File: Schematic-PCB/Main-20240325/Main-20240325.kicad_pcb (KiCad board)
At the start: 4 copper layers, 112 x 112 mm, 102 parts, among them J1 Conn_PWR, J2 CamS3-4, J3 CamS3-6, J4 Pixy 2.1, J5 Conn_MD, J6 Conn_Dribbler, J7 Conn_UI, J8 Conn_NeoPixel, SW1 Cam_RST, SW2 Main_RST, SW3 Sub_RST, SW4 SW_DPDT_x2, U1 DEV-16771, U10 TSSP4038, U11 TSSP4038, U12 TSSP4038, U13 TSSP4038, U14 TSSP4038, U15 TSSP4038, U16 TSSP4038, U17 TSSP4038, U19 ESP32-DEVKITC, U2 TSSP4038, U20 TSSP4038, U21 TSSP4038, U22 TSSP4038, U23 TSSP4038, U3 TSSP4038, U4 TSSP4038, U5 TSSP4038, U6 TSSP4038, U7 TSSP4038, U8 TSSP4038, U9 TSSP4038

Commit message: update: メイン基板を更新した
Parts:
- removed R28: 10, Resistor_SMD:R_0603_1608Metric
- removed R29: 510, Resistor_SMD:R_0603_1608Metric
- RV1: value 1K -> 10K
- moved U1 1.09 mm to (0.00, -1.09)
- moved U19 1.09 mm to (0.00, -1.09)
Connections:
- net Volume renamed Net-(R30-Pad1)
- J3 pad 1: Cam-EN -> unconnected-(J3-Pin_1-Pad1)
- J3 pad 2: unconnected-(J3-Pin_2-Pad2) -> Cam-EN
- RV1 pad 1: Net-(R28-Pad2) -> +3.3V
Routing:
- net +3.3V: track 59.0 -> 85.2 mm
- net Net-(R28-Pad2): track 3.00 -> 0.00 mm
- net Net-(R28-Pad1): track 2.00 -> 0.00 mm
- net SDA: track 19.9 -> 21.0 mm
- net SCL: track 25.3 -> 26.4 mm

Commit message: clean: コンフリクトを修正
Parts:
- removed J8: Conn_NeoPixel, @2024TOINIOT2-Main:Connector
- added REF**: MountingHole_3.2mm_M3, MountingHole:MountingHole_3.2mm_M3, F.Cu at (23.6, -35.3)
- added REF**: MountingHole_3.2mm_M3, MountingHole:MountingHole_3.2mm_M3, F.Cu at (23.6, 35.3)
- added REF**: MountingHole_3.2mm_M3, MountingHole:MountingHole_3.2mm_M3, F.Cu at (-23.7, -35.5)
- moved J6 3.40 mm to (22.6, -19.7)
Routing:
- net +5V: track 49.9 -> 46.3 mm
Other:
- board text removed: "A0"
- board text removed: "A1"
- board text removed: "A12"
- board text removed: "A13"
- board text removed: "A14"
- board text removed: "A15"
- board text removed: "A16"
- board text removed: "A17"
- board text removed: "A2"
- board text removed: "A3"
- board text removed: "A4"
- board text removed: "A5"
- board text removed: "A6"
- board text removed: "A7"
- board text removed: "A8"
- board text removed: "A9"

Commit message: update: メイン基板のPCBで部品配置を進めた
ESP32C3にしたら結構配置がいい感じに決まった...のか？
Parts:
- removed R26, R27: 330, Resistor_SMD:R_0603_1608Metric
- removed the REF** at (30.1, -30.1)
- removed the REF** at (30.1, 30.1)
- removed the REF** at (23.6, -35.3)
- removed the REF** at (23.6, 35.3)
- removed the REF** at (-23.7, -35.5)
- removed the REF** at (-30.1, 30.1)
- removed the REF** at (-30.1, -30.1)
- removed SW3: Sub_RST, @2024TOINIOT2-Line:Tactile1
- removed U20, U21, U22, U23: TSSP4038, OptoDevice:Vishay_MINICAST-3Pin
- added J8: Conn_NeoPixel, @2024TOINIOT2-Main:Connector, F.Cu at (0.00, -46.0)
- added REF**: MountingHole_3.2mm_M3, MountingHole:MountingHole_3.2mm_M3, F.Cu at (30.1, 30.1)
- added REF**: MountingHole_3.2mm_M3, MountingHole:MountingHole_3.2mm_M3, F.Cu at (-30.1, 30.1)
- added REF**: MountingHole_3.2mm_M3, MountingHole:MountingHole_3.2mm_M3, F.Cu at (-23.6, -35.3)
- added REF**: MountingHole_3.2mm_M3, MountingHole:MountingHole_3.2mm_M3, F.Cu at (23.6, -35.3)
- added REF**: MountingHole_3.2mm_M3, MountingHole:MountingHole_3.2mm_M3, F.Cu at (23.6, 35.3)
- added REF**: MountingHole_3.2mm_M3, MountingHole:MountingHole_3.2mm_M3, F.Cu at (-23.6, 35.3)
- added REF**: MountingHole_3.2mm_M3, MountingHole:MountingHole_3.2mm_M3, F.Cu at (30.1, -30.1)
- added REF**: MountingHole_3.2mm_M3, MountingHole:MountingHole_3.2mm_M3, F.Cu at (-30.1, -30.1)
- added SW5: Cam_RST, @2024TOINIOT2-Line:Tactile1, F.Cu at (186.5, 120.0)
- C1, C2: moved to F.Cu
- C10, C11, C12, C9: value 0.33uF -> 0.1uF
- D1: value PWR-5 -> BLTIN; footprint LED_SMD:LED_0805_2012Metric -> LED_SMD:LED_0603_1608Metric
- D2: value PWR-3.3 -> BLTIN; footprint LED_SMD:LED_0805_2012Metric -> LED_SMD:LED_0603_1608Metric
- D3: value D_Small -> PWR-5; footprint Diode_THT:D_A-405_P7.62mm_Horizontal -> LED_SMD:LED_0603_1608Metric
- D4: value BLTIN -> PWR-3.3
- D5: value BLTIN -> D_Small; footprint LED_SMD:LED_0603_1608Metric -> Diode_THT:D_A-405_P7.62mm_Horizontal
- J3: footprint Connector_PinSocket_2.54mm:PinSocket_2x03_P2.54mm_Vertical -> Connector_PinHeader_2.54mm:PinHeader_2x03_P2.54mm_Vertical
- R1: value 10K -> 330
- R16, R17, R6: value 39K -> 10K
- R20, R21: value 1K -> 39K
- R3: value 330 -> 1K
- R4: value 39K -> 1K
- R5, R7: value 39K -> 330
- RV1: footprint @2024-Main:3362P -> @2024TOINIOT2-Main:3362P
- SW1: value Cam_RST -> SW_DPDT_x2; footprint @2024TOINIOT2-Line:Tactile1 -> @2024TOINIOT2-Main:2MD1-T2-B4-M2-Q-N; moved to B.Cu
- SW4: value SW_DPDT_x2 -> Cam_RST; footprint @2024-Main:2MD1T2B4M2QN -> @2024TOINIOT2-Line:Tactile1; moved to F.Cu
- U10, U11, U12, U13, U14, U15, U16, U17, U3, U4, U5, U6, U7, U8, U9: footprint @2024TOINIOT2-Main:Vishay_MINICAST-3Pin -> @2024TOINIOT2-Main:TSSP4038
- U18: value ~ -> TSSP4038; footprint @2024TOINIOT2-Main:BNO055 -> @2024TOINIOT2-Main:TSSP4038
- U19: value ESP32-DEVKITC -> ~; footprint @2024TOINIOT2-Main:ESP32-DEVKITC -> @2024TOINIOT2-Main:XIAO ESP32C3
- U2: value TSSP4038 -> ~; footprint @2024TOINIOT2-Main:Vishay_MINICAST-3Pin -> @2024TOINIOT2-Main:BNO055; moved to F.Cu
- moved SW4 237.2 mm to (186.5, 114.5), turned to 0 degrees
- moved C2 225.5 mm to (161.8, 123.7)
- moved C1 213.3 mm to (161.8, 112.1)
- moved SW2 188.0 mm to (186.5, 109.0), turned to 0 degrees
- moved RV1 173.0 mm to (162.4, 133.7), turned to 0 degrees
- moved D3 165.7 mm to (134.0, 131.8), turned to 0 degrees
- moved SW1 72.0 mm to (-33.3, 22.2), turned to 123.75 degrees
- moved D1 49.7 mm to (134.0, 126.6)
- moved U18 49.5 mm to (18.9, -45.7), turned to -22.5 degrees
- moved D2 49.3 mm to (134.0, 129.2)
- moved D5 46.1 mm to (181.3, 90.5)
- moved J4 41.1 mm to (-16.3, -5.08), turned to 0 degrees
- moved J2 38.9 mm to (-12.0, 21.0)
- moved J3 38.0 mm to (-17.5, 15.3)
- moved U2 33.8 mm to (17.0, -20.3)
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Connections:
- C10 pad 1: ball02 -> +3.3V
- C11 pad 1: ball03 -> +5V
- C12 pad 1: ball04 -> +5V
- C13 pad 1: ball05 -> ball01
- C14 pad 1: ball06 -> ball02
- C15 pad 1: ball07 -> ball03
- C16 pad 1: ball08 -> ball04
- C17 pad 1: ball09 -> ball05
- C18 pad 1: ball10 -> ball06
- C19 pad 1: ball11 -> ball07
- C20 pad 1: ball12 -> ball08
- C21 pad 1: ball13 -> ball09
- C22 pad 1: ball14 -> ball10
- C23 pad 1: ball15 -> ball11
- C24 pad 1: ball16 -> ball12
- C25 pad 1: ball-a-01 -> ball13
- C26 pad 1: ball-a-02 -> ball14
- C27 pad 1: ball-a-03 -> ball15
- C28 pad 1: ball-a-04 -> ball16
- C9 pad 1: ball01 -> +5V
- D3 pad 1: Net-(D3-K) -> GND
- D3 pad 2: +5V -> Net-(D3-A)
- D5 pad 1: GND -> Net-(D5-K)
- D5 pad 2: Net-(D5-A) -> +5V
- J3 pad 1: unconnected-(J3-Pin_1-Pad1) -> Cam_EN
- J3 pad 2: Cam-EN -> Cam_G0
- J3 pad 4: +5V -> Cam-RX
- J3 pad 6: Cam-RX -> +5V
- R1 pad 1: +5V -> SCK
- R1 pad 2: Cam-EN -> Net-(D1-A)
- R10 pad 1: Net-(U8-OUT) -> Net-(U5-OUT)
- R10 pad 2: ball07 -> ball03
- R11 pad 1: Net-(U9-OUT) -> Net-(U6-OUT)
- R11 pad 2: ball08 -> ball04
- R12 pad 1: Net-(U10-OUT) -> Net-(U7-OUT)
- R12 pad 2: ball09 -> ball05
- R13 pad 1: Net-(U11-OUT) -> Net-(U8-OUT)
- R13 pad 2: ball10 -> ball06
- R14 pad 1: Net-(U12-OUT) -> Net-(U9-OUT)
- R14 pad 2: ball11 -> ball07
- R15 pad 1: Net-(U13-OUT) -> Net-(U10-OUT)
- R15 pad 2: ball12 -> ball08
- R16 pad 1: Net-(U14-OUT) -> +3.3V
- R16 pad 2: ball13 -> Cam_EN
- R17 pad 1: Net-(U15-OUT) -> +3.3V
- R17 pad 2: ball14 -> Cam_G0
- R18 pad 1: Net-(U16-OUT) -> Net-(U11-OUT)
- R18 pad 2: ball15 -> ball09
- R19 pad 1: Net-(U17-OUT) -> Net-(U12-OUT)
- R19 pad 2: ball16 -> ball10
- R2 pad 1: +5V -> Sub_BLTIN
- R2 pad 2: Net-(D1-A) -> Net-(D2-A)
- R20 pad 1: +3.3V -> Net-(U13-OUT)
- R20 pad 2: SDA -> ball11
- R21 pad 1: +3.3V -> Net-(U14-OUT)
- R21 pad 2: SCL -> ball12
- R22 pad 1: Net-(U20-OUT) -> Net-(U15-OUT)
- R22 pad 2: ball-a-01 -> ball13
- R23 pad 1: Net-(U21-OUT) -> Net-(U16-OUT)
- R23 pad 2: ball-a-02 -> ball14
- R24 pad 1: Net-(U22-OUT) -> Net-(U17-OUT)
- R24 pad 2: ball-a-03 -> ball15
- R25 pad 1: Net-(U23-OUT) -> Net-(U18-OUT)
- R25 pad 2: ball-a-04 -> ball16
- R3 pad 2: Net-(D2-A) -> SDA
- R4 pad 1: Net-(U2-OUT) -> +3.3V
- R4 pad 2: ball01 -> SCL
- R5 pad 1: Net-(U3-OUT) -> +5V
- R5 pad 2: ball02 -> Net-(D3-A)
- R6 pad 1: Net-(U4-OUT) -> Net-(R6-Pad1)
- R6 pad 2: ball03 -> Volume
- R7 pad 1: Net-(U5-OUT) -> +3.3V
- R7 pad 2: ball04 -> Net-(D4-A)
- R8 pad 1: Net-(U6-OUT) -> Net-(U3-OUT)
- R8 pad 2: ball05 -> ball01
- R9 pad 1: Net-(U7-OUT) -> Net-(U4-OUT)
- R9 pad 2: ball06 -> ball02
- RV1 pad 2: Net-(R30-Pad1) -> Net-(R6-Pad1)
- SW1 pad 1: GND -> +5V
- SW1 pad 2: Cam-EN -> 5.0V
- SW4 pad 1: +5V -> GND
- SW4 pad 2: 5.0V -> Cam_EN
- U1 pad 3.3V: +3.3V -> unconnected-(U1-Pad3.3V)
- U18 pad 1: +3.3V -> Net-(U18-OUT)
- U18 pad 3: SDA -> +3.3V
- U19 pad 1: unconnected-(U19-3V3-Pad1) -> ball01k
- U19 pad 10: KickerSignal -> unconnected-(U19-MISO_D9-Pad10)
- U19 pad 11: PH-D -> NeoPixel_PWM
- U19 pad 12: EN-D -> unconnected-(U19-3V3-Pad12)
- U19 pad 13: unconnected-(U19-12_A15-Pad13) -> GND
- U19 pad 14: GND -> Net-(D5-K)
- U19 pad 2: Sub_RST -> ball02k
- U19 pad 3: ball01k -> KickerSignal
- U19 pad 4: ball02k -> Volume
- U19 pad 5: ball-a-01 -> PH-D
- U19 pad 6: ball-a-02 -> EN-D
- U19 pad 7: ball-a-03 -> Main-RX7
- U19 pad 8: ball-a-04 -> Main-TX7
- U19 pad 9: NeoPixel_PWM -> Sub_BLTIN
- U2 pad 1: Net-(U2-OUT) -> +3.3V
- U2 pad 3: +3.3V -> SDA
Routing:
- net +3.3V: track 85.2 -> 0.00 mm
- net +5V: track 46.3 -> 0.00 mm
- net 3.3V: track 22.6 -> 0.00 mm
- net SCL: track 26.4 -> 9.93 mm
- net SDA: track 21.0 -> 9.93 mm
- net 5.0V: track 9.33 -> 0.00 mm
- removed copper zone on B.Cu, net GND
- removed copper zone on F.Cu, net GND
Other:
- outline, holes or cut-outs redrawn

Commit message: update: メイン基板の回路図/PCBを更新
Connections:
- U19 pad 3: KickerSignal -> Volume
- U19 pad 4: Volume -> KickerSignal

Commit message: update: 部品配置を進めた
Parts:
- C1, C2: moved to B.Cu
- moved C2 232.0 mm to (-29.9, -7.05)
- moved C1 219.8 mm to (-29.9, 4.50)
- moved SW5 186.3 mm to (37.5, 8.20), turned to 180 degrees
- moved SW4 180.0 mm to (37.5, 13.7), turned to 180 degrees
- moved RV1 179.9 mm to (42.0, 0.00), turned to 90 degrees
- moved SW2 174.1 mm to (37.5, 19.1), turned to 180 degrees

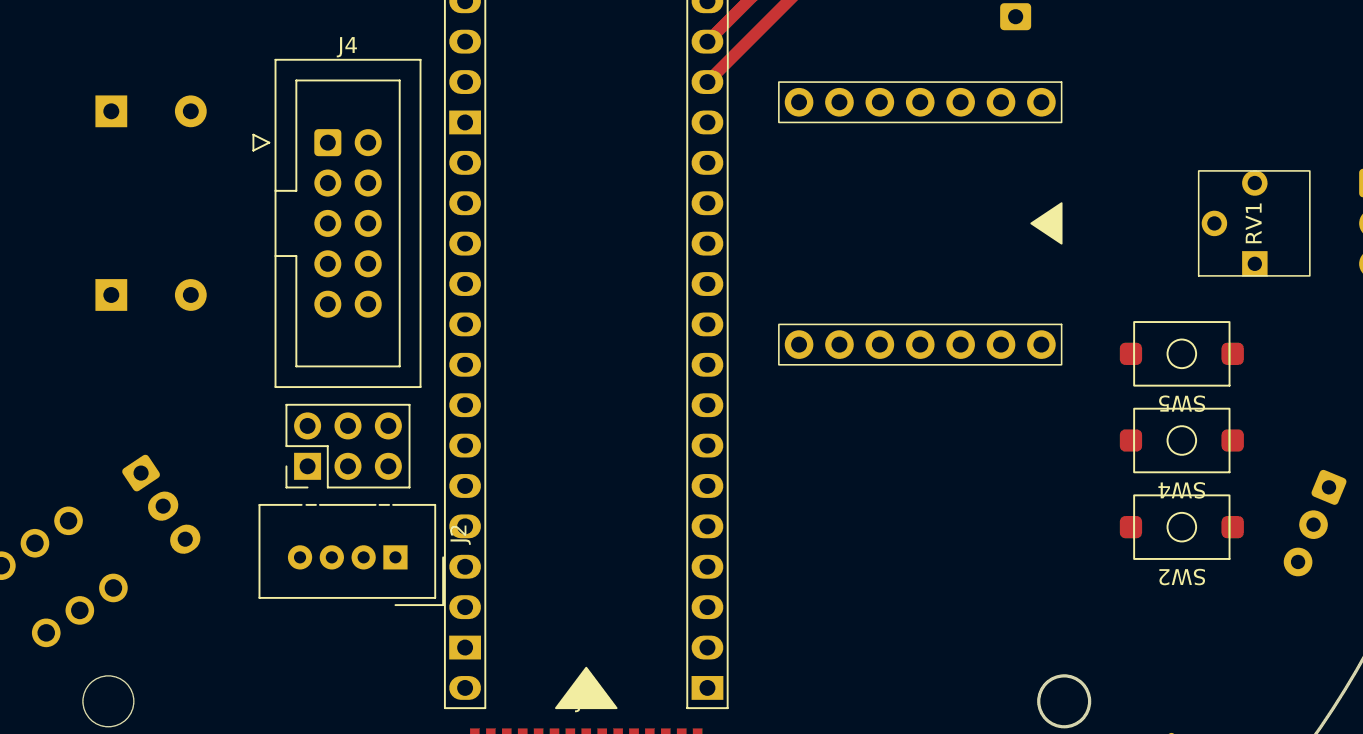
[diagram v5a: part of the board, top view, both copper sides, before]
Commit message: update: メイン基板のコンデンサの型番を変更した
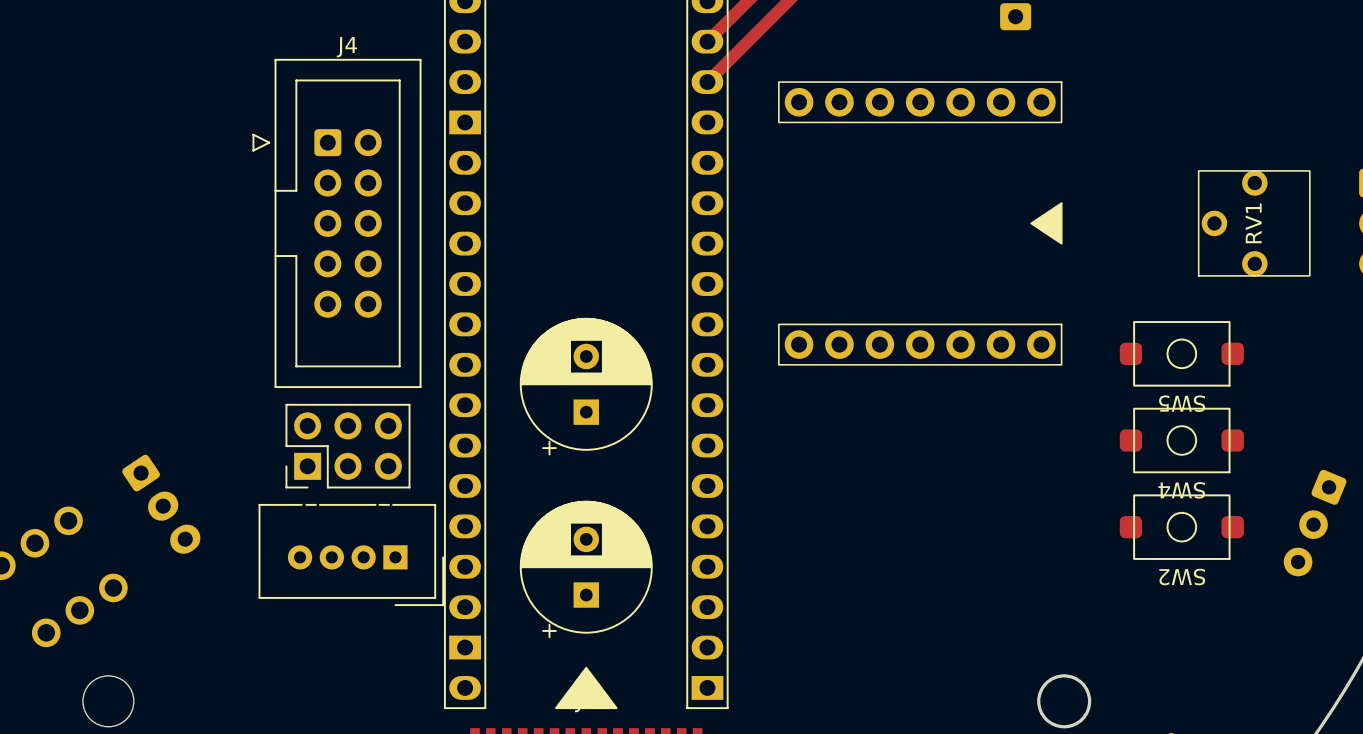
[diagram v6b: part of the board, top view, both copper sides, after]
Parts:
- C1, C2: value 1000uF -> 470uF; footprint Capacitor_THT:CP_Radial_D10.0mm_P5.00mm -> Capacitor_THT:CP_Radial_D8.0mm_P3.50mm; moved to F.Cu
- moved C2 42.6 mm to (0.00, 23.4), turned to 90 degrees
- moved C1 30.8 mm to (0.00, 11.9), turned to 90 degrees

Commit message: update: メイン基板のPCBデザインを少しすすめた
配線終わらないぞー
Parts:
- moved J7 22.5 mm to (-37.0, 11.2), turned to 90 degrees
- moved C1 11.5 mm to (0.00, 23.4)
- moved C2 11.5 mm to (0.00, 11.9)
- moved RV1 4.54 mm to (37.5, 0.00)
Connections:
- U1 pad 30: SW-TAC-4 -> SW-TAC-2
- U1 pad 32: SW-TAC-2 -> SW-TAC-4
- U1 pad 36: SW-TOG -> SW-TAC-1
- U1 pad 37: SW-TAC-1 -> SW-TOG
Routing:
- net +5V: track 0.00 -> 87.1 mm
- net SW-TAC-4: track 0.00 -> 56.1 mm
- net SW-TAC-3: track 0.00 -> 56.1 mm
- net SW-TAC-2: track 0.00 -> 56.1 mm
- net SW-TAC-1: track 0.00 -> 39.9 mm
- net SW-TOG: track 0.00 -> 39.8 mm
- net BUZZER: track 0.00 -> 36.8 mm
- net Main-TX7: track 0.00 -> 31.6 mm, vias 0 -> 1
- net SS: track 0.00 -> 31.3 mm
- net MISO: track 0.00 -> 26.6 mm
- net MOSI: track 0.00 -> 22.9 mm
- net SCK: track 0.00 -> 15.7 mm
- net Main-RX7: track 0.00 -> 15.3 mm
- net EN-D: track 0.00 -> 14.3 mm
- net PH-D: track 0.00 -> 10.8 mm
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- added copper zone on In1.Cu, net +3.3V
- added copper zone on B.Cu, net GND
- added copper zone on F.Cu, net GND

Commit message: Auto stash before merge of "main" and "origin/main"
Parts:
- added C27: 0.1uF, Capacitor_SMD:C_0603_1608Metric, F.Cu at (97.7, 9.66)
- added J6: Conn_NeoPixel, @2024TOINIOT2-Main:Connector, F.Cu at (84.4, 26.6)
- renumbered C21 to C13
